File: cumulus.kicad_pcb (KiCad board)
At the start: 2 copper layers, 153.9 x 127.6 mm, 43 parts

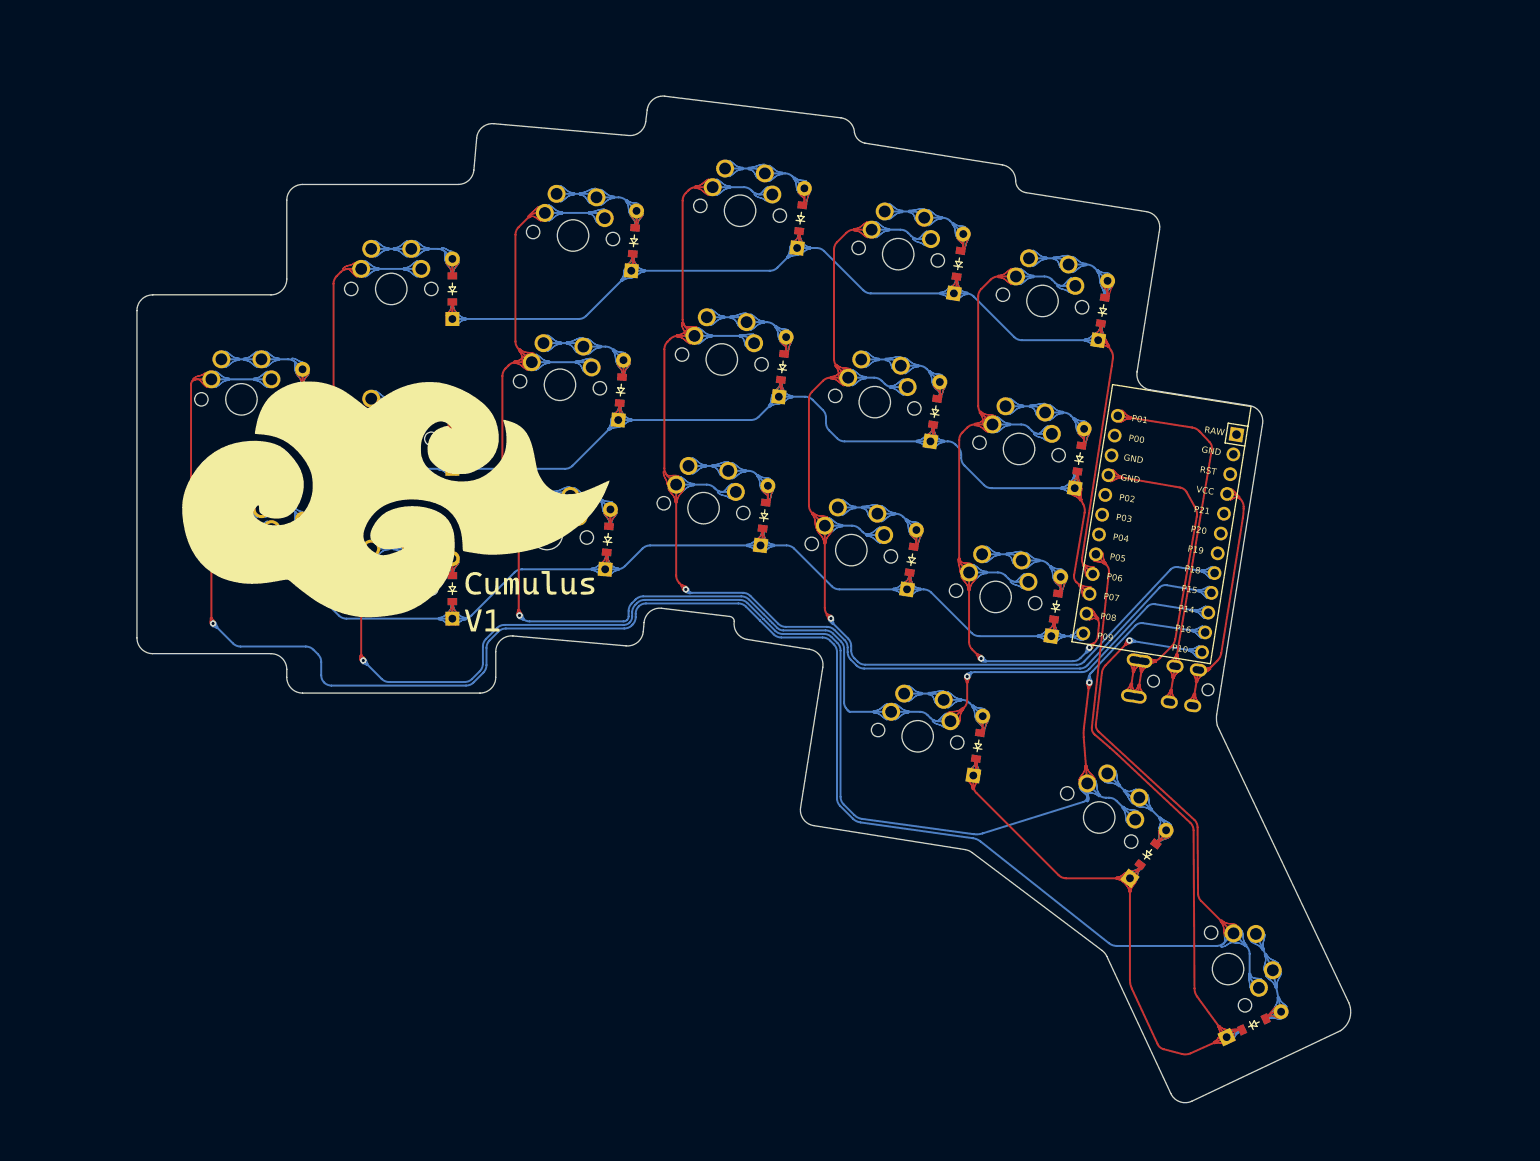
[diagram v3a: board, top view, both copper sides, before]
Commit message: Logo + PCB fill zone
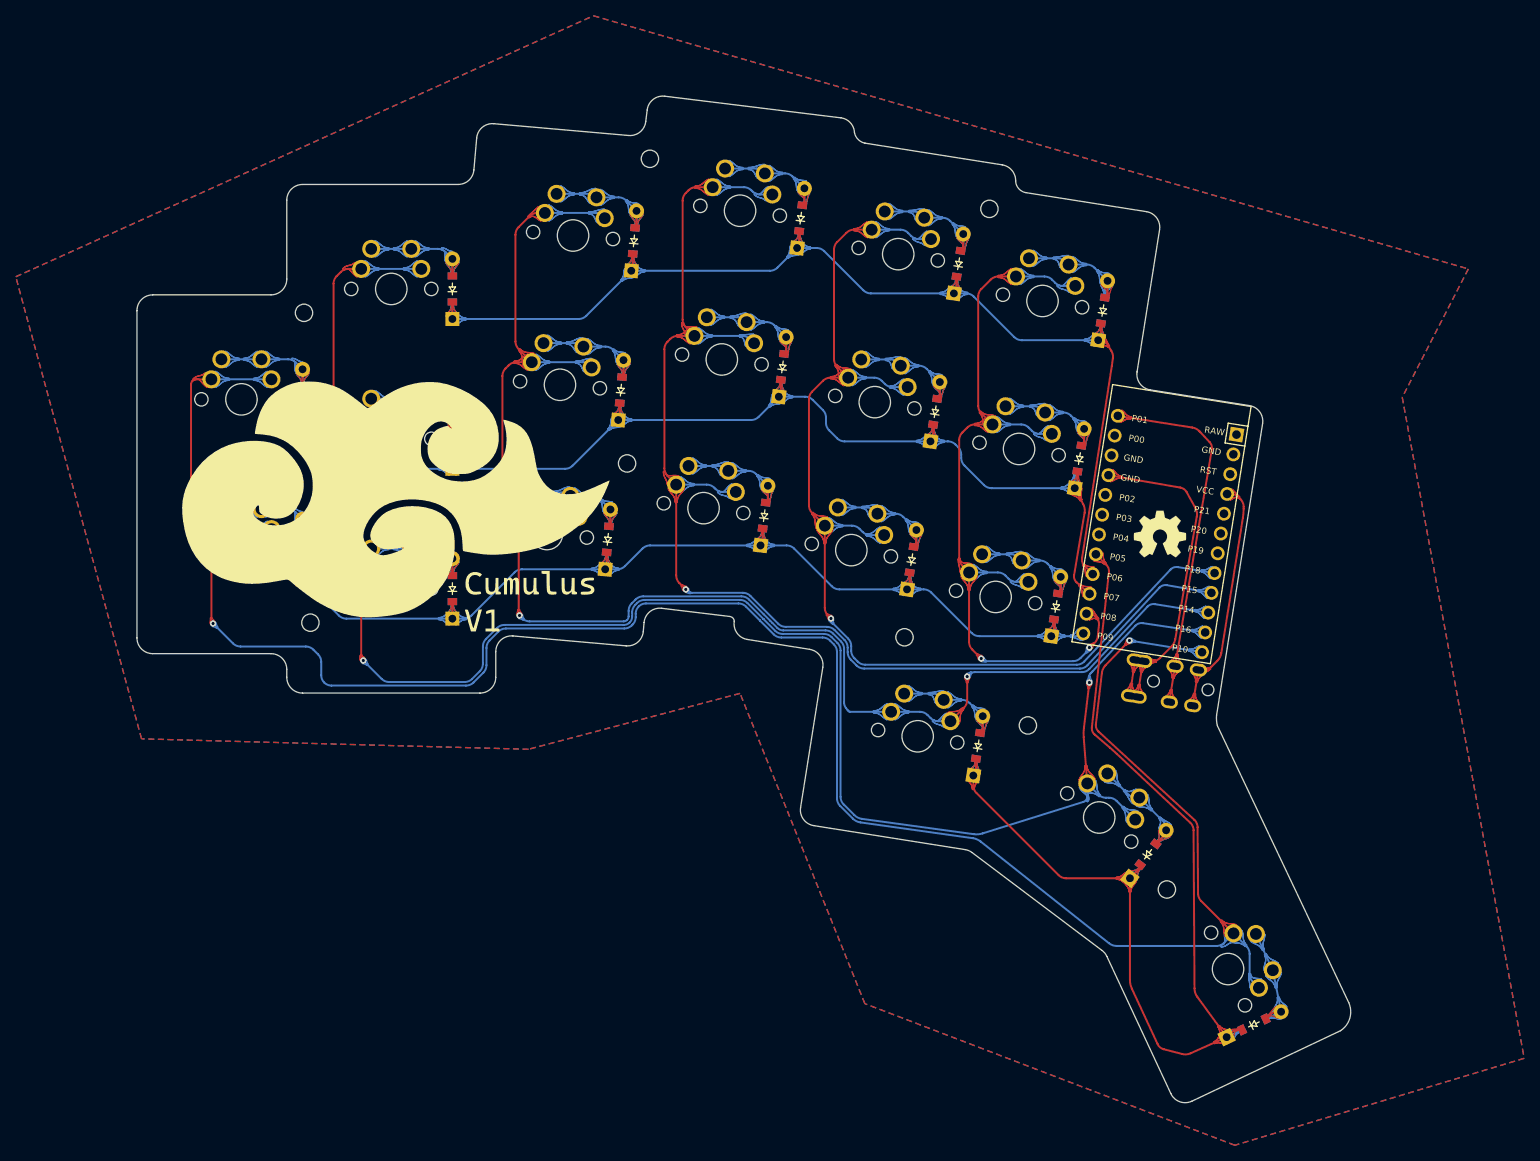
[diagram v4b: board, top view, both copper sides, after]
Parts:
- added REF**: MountingHole_2.2mm_M2, MountingHole:MountingHole_2.2mm_M2, F.Cu at (155.8, 107.4)
- added REF**: MountingHole_2.2mm_M2, MountingHole:MountingHole_2.2mm_M2, F.Cu at (156.6, 146.7)
- added REF**: MountingHole_2.2mm_M2, MountingHole:MountingHole_2.2mm_M2, F.Cu at (199.7, 87.9)
- added REF**: MountingHole_2.2mm_M2, MountingHole:MountingHole_2.2mm_M2, F.Cu at (265.2, 180.5)
- added REF**: MountingHole_2.2mm_M2, MountingHole:MountingHole_2.2mm_M2, F.Cu at (247.6, 159.7)
- added REF**: MountingHole_2.2mm_M2, MountingHole:MountingHole_2.2mm_M2, F.Cu at (232.0, 148.6)
- added REF**: MountingHole_2.2mm_M2, MountingHole:MountingHole_2.2mm_M2, F.Cu at (196.8, 126.5)
- added REF**: OSHW-Symbol_6.7x6mm_SilkScreen, Symbol:OSHW-Symbol_6.7x6mm_SilkScreen, F.Cu at (264.3, 135.5)
- added REF**: MountingHole_2.2mm_M2, MountingHole:MountingHole_2.2mm_M2, F.Cu at (242.7, 94.2)
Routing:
- added copper zone on B.Cu, net GND
- added copper zone on F.Cu, net GND
